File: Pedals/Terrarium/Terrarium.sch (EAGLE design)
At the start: 7 parts, among them U1 ES_DAISY_SEED

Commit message: Updating schematic
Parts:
- added C1: 100p, capacitors-film:CAP.5
- added C100: 100u, capacitors-elec:5.0_MM.4
- added C2, C3, C6: 1u, capacitors-film:CAP.6
- added C4, C5, C8, C9: 100n, capacitors-film:CAP.5
- added C7: 1n, capacitors-film:CAP.5
- added D100: 1N5817, diodes:DO41.3
- added FS1, FS2, SW1, SW2, SW3, SW4: SPST, switches:SPST
- added GND, PWR: PADRD, supply pins:PADRD
- added IC1: TL072CP, SamacSys_Parts:TL072CP
- added IC2: L78L05CZ, SamacSys_Parts:L78L05CZ
- added LED1, LED2: LED.3, diodes:LED.3
- added R5, R8: 1k, SparkFun-Resistors:1KOHM-HORIZ-1/4W-1%
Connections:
- new net +5V: C5.1, C9.1, IC2.VOUT
- new net FS1: FS1.P, U1.GPIO25(ADC10)
- new net FS2: FS2.P, U1.GPIO26(SAI2_SD_A)
- new net IC1_1: IC1.1OUT
- new net IC1_2: IC1.1IN-
- new net IC1_3: IC1.1IN+
- new net IC1_4: IC1.VCC-
- new net IC1_5: IC1.2IN+
- new net IC1_6: IC1.2IN-
- new net IC1_7: IC1.2OUT
- new net IC1_8: IC1.VCC+
- new net LED1: R5.2, U1.GPIO22(ADC7/DAC2)
- new net LED2: R8.2, U1.GPIO23(ADC8/DAC1)
- new net LEFT_IN: U1.AUDIO_IN_L
- new net LEFT_OUT: U1.AUDIO_OUT_L
- new net N$7: LED1.A, R5.1
- new net N$8: LED2.A, R8.1
- new net N$9: D100.A, PWR.P$1
- new net SW1: SW1.P, U1.GPIO10(SPI1_MOSI)
- new net SW2: SW2.P, U1.GPIO9(SPI1_MISO)
- new net SW3: SW3.P, U1.GPIO8(SPI1_SCK)
- new net SW4: SW4.P, U1.GPIO7(SPI1_NSS)
- net GND: now also C100.-, C4.2, C5.2, C8.2, C9.2, FS1.S, FS2.S, GND.P$1, IC2.GND, LED1.C, LED2.C, SW1.S, SW2.S, SW3.S, SW4.S
- net VCC: now also C100.+, C4.1, C8.1, D100.C, IC2.VIN

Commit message: Finish base schematic
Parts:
- added IN, IN_GND, OUT, OUT_GND: PADRD, supply pins:PADRD
- added R1, R2, R3, R9: 1M, resistors:R.3B
- added R4: 100R, resistors:R.3B
- added R6: 100K, resistors:R.3B
- added R7: 1K, resistors:R.3B
- POT1, POT2, POT3, POT4, POT5, POT6: value (none) -> B10K
- R5, R8: value 1k -> 1K; device SparkFun-Resistors:1KOHM-HORIZ-1/4W-1% -> resistors:R.3B
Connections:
- removed net IC1_1: IC1.1OUT
- removed net IC1_2: IC1.1IN-
- removed net IC1_3: IC1.1IN+
- removed net IC1_4: IC1.VCC-
- removed net IC1_5: IC1.2IN+
- removed net IC1_6: IC1.2IN-
- removed net IC1_7: IC1.2OUT
- removed net IC1_8: IC1.VCC+
- new net N$10: C3.2, R4.1
- new net N$11: C3.1, OUT.P$1, R6.1
- new net N$12: C1.1, C6.2, IN.P$1
- new net N$14: IC1.2IN-, IC1.2OUT, R4.2
- new net N$15: C6.1, R7.2
- new net N$16: C7.1, IC1.1IN+, R1.2, R3.1, R7.1
- new net N$17: C2.1, IC1.2IN+, R2.1, R9.2
- net +5V: now also IC1.VCC+, R1.1, R2.2
- net GND: now also C1.2, C7.2, IC1.VCC-, IN_GND.P$1, OUT_GND.P$1, R3.2, R6.2, R9.1
- net LEFT_IN: now also IC1.1IN-, IC1.1OUT
- net LEFT_OUT: now also C2.2
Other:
- moved on the sheet: C1, C100, C2, C3, C4, C5, C6, C7, C8, C9, D100, IC1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

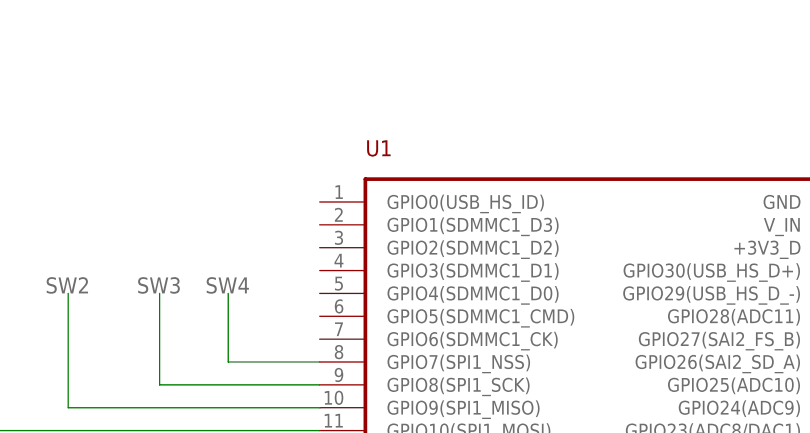
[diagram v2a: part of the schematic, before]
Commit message: Begin board layout
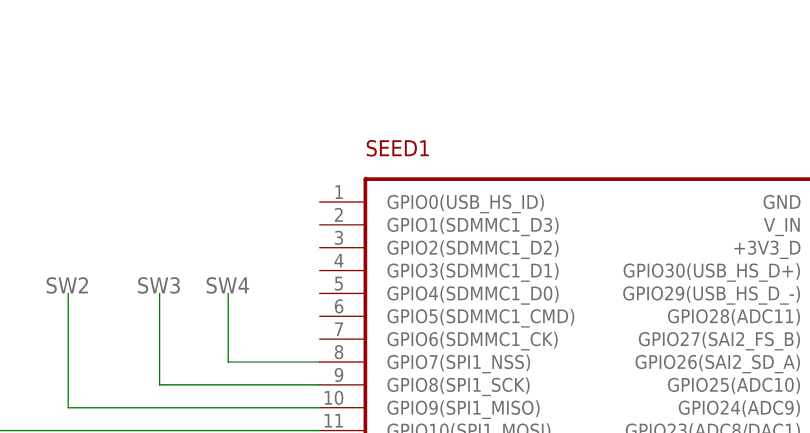
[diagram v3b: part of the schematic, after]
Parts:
- renumbered U1 to SEED1
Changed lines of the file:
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@@
 </classes>
 <parts>
-<part name="U1" library="Electrosmith_Boards" deviceset="ES_DAISY_SEED" device=""/>
+<part name="SEED1" library="Electrosmith_Boards" deviceset="ES_DAISY_SEED" device=""/>
 <part name="GND1" library="SparkFun-PowerSymbols" library_urn="urn:adsk.eagle:library:530" deviceset="GND" device=""/>
 <part name="GND2" library="SparkFun-PowerSymbols" library_urn="urn:adsk.eagle:library:530" deviceset="GND" device=""/>
@@
 </plain>
 <instances>
-<instance part="U1" gate="G$1" x="66.04" y="53.34" smashed="yes">
+<instance part="SEED1" gate="G$1" x="66.04" y="53.34" smashed="yes">
 <attribute name="NAME" x="40.64" y="81.28" size="1.778" layer="94"/>
 <attribute name="VALUE" x="91.44" y="22.86" size="1.778" layer="94" rot="R180"/>
@@
 <segment>
 <wire x1="104.14" y1="81.28" x2="104.14" y2="73.66" width="0.1524" layer="91"/>
-<pinref part="U1" gate="G$1" pin="V_IN"/>
+<pinref part="SEED1" gate="G$1" pin="V_IN"/>
 <wire x1="104.14" y1="73.66" x2="96.52" y2="73.66" width="0.1524" layer="91"/>
 <label x="101.6" y="81.28" size="1.778" layer="95"/>
@@
 <net name="3V3_D" class="0">
 <segment>
-<pinref part="U1" gate="G$1" pin="+3V3_D"/>
+<pinref part="SEED1" gate="G$1" pin="+3V3_D"/>
 <wire x1="96.52" y1="71.12" x2="111.76" y2="71.12" width="0.1524" layer="91"/>
 <wire x1="111.76" y1="71.12" x2="111.76" y2="81.28" width="0.1524" layer="91"/>
@@
 <net name="GND" class="0">
 <segment>
-<pinref part="U1" gate="G$1" pin="GND"/>
+<pinref part="SEED1" gate="G$1" pin="GND"/>
 <wire x1="96.52" y1="76.2" x2="129.54" y2="76.2" width="0.1524" layer="91"/>
 <pinref part="GND1" gate="1" pin="GND"/>
@@
 </segment>
 <segment>
-<pinref part="U1" gate="G$1" pin="AGND"/>
+<pinref part="SEED1" gate="G$1" pin="AGND"/>
 <wire x1="35.56" y1="27.94" x2="27.94" y2="27.94" width="0.1524" layer="91"/>
 <pinref part="GND2" gate="1" pin="GND"/>
@@
 <net name="3V3_A" class="0">
 <segment>
-<pinref part="U1" gate="G$1" pin="+3V3_A"/>
+<pinref part="SEED1" gate="G$1" pin="+3V3_A"/>
 <wire x1="96.52" y1="27.94" x2="111.76" y2="27.94" width="0.1524" layer="91"/>
 <label x="106.68" y="27.94" size="1.778" layer="95"/>
@@
 <net name="N$1" class="0">
 <segment>
-<pinref part="U1" gate="G$1" pin="GPIO16(ADC1)"/>
+<pinref part="SEED1" gate="G$1" pin="GPIO16(ADC1)"/>
 <pinref part="POT1" gate="G$1" pin="2"/>
 <wire x1="96.52" y1="33.02" x2="127" y2="33.02" width="0.1524" layer="91"/>
@@
 <net name="N$2" class="0">
 <segment>
-<pinref part="U1" gate="G$1" pin="GPIO17(ADC2)"/>
+<pinref part="SEED1" gate="G$1" pin="GPIO17(ADC2)"/>
 <pinref part="POT2" gate="G$1" pin="2"/>
 <wire x1="96.52" y1="35.56" x2="142.24" y2="35.56" width="0.1524" layer="91"/>
@@
 <net name="N$3" class="0">
 <segment>
-<pinref part="U1" gate="G$1" pin="GPIO18(ADC3)"/>
+<pinref part="SEED1" gate="G$1" pin="GPIO18(ADC3)"/>
 <pinref part="POT3" gate="G$1" pin="2"/>
 <wire x1="96.52" y1="38.1" x2="157.48" y2="38.1" width="0.1524" layer="91"/>
@@
 <net name="N$4" class="0">
 <segment>
-<pinref part="U1" gate="G$1" pin="GPIO19(ADC4)"/>
+<pinref part="SEED1" gate="G$1" pin="GPIO19(ADC4)"/>
 <pinref part="POT4" gate="G$1" pin="2"/>
 <wire x1="96.52" y1="40.64" x2="172.72" y2="40.64" width="0.1524" layer="91"/>
@@
 <net name="N$5" class="0">
 <segment>
-<pinref part="U1" gate="G$1" pin="GPIO20(ADC5)"/>
+<pinref part="SEED1" gate="G$1" pin="GPIO20(ADC5)"/>
 <pinref part="POT5" gate="G$1" pin="2"/>
 <wire x1="96.52" y1="43.18" x2="187.96" y2="43.18" width="0.1524" layer="91"/>
@@
 <net name="N$6" class="0">
 <segment>
-<pinref part="U1" gate="G$1" pin="GPIO21(ADC6)"/>
+<pinref part="SEED1" gate="G$1" pin="GPIO21(ADC6)"/>
 <pinref part="POT6" gate="G$1" pin="2"/>
 <wire x1="96.52" y1="45.72" x2="205.74" y2="45.72" width="0.1524" layer="91"/>
@@
 <net name="FS2" class="0">
 <segment>
-<pinref part="U1" gate="G$1" pin="GPIO26(SAI2_SD_A)"/>
+<pinref part="SEED1" gate="G$1" pin="GPIO26(SAI2_SD_A)"/>
 <wire x1="96.52" y1="58.42" x2="101.6" y2="58.42" width="0.1524" layer="91"/>
 <wire x1="101.6" y1="58.42" x2="101.6" y2="63.5" width="0.1524" layer="91"/>
@@
 <net name="FS1" class="0">
 <segment>
-<pinref part="U1" gate="G$1" pin="GPIO25(ADC10)"/>
+<pinref part="SEED1" gate="G$1" pin="GPIO25(ADC10)"/>
 <wire x1="96.52" y1="55.88" x2="106.68" y2="55.88" width="0.1524" layer="91"/>
 <wire x1="106.68" y1="55.88" x2="106.68" y2="63.5" width="0.1524" layer="91"/>
@@
 <net name="LED2" class="0">
 <segment>
-<pinref part="U1" gate="G$1" pin="GPIO23(ADC8/DAC1)"/>
+<pinref part="SEED1" gate="G$1" pin="GPIO23(ADC8/DAC1)"/>
 <wire x1="96.52" y1="50.8" x2="114.3" y2="50.8" width="0.1524" layer="91"/>
 <wire x1="114.3" y1="50.8" x2="114.3" y2="63.5" width="0.1524" layer="91"/>
@@
 <net name="LED1" class="0">
 <segment>
-<pinref part="U1" gate="G$1" pin="GPIO22(ADC7/DAC2)"/>
+<pinref part="SEED1" gate="G$1" pin="GPIO22(ADC7/DAC2)"/>
 <wire x1="96.52" y1="48.26" x2="121.92" y2="48.26" width="0.1524" layer="91"/>
 <wire x1="121.92" y1="48.26" x2="121.92" y2="63.5" width="0.1524" layer="91"/>
@@
 <net name="LEFT_OUT" class="0">
 <segment>
-<pinref part="U1" gate="G$1" pin="AUDIO_OUT_L"/>
+<pinref part="SEED1" gate="G$1" pin="AUDIO_OUT_L"/>
 <wire x1="35.56" y1="33.02" x2="10.16" y2="33.02" width="0.1524" layer="91"/>
 <label x="5.08" y="33.02" size="1.778" layer="95"/>
@@
 <net name="LEFT_IN" class="0">
 <segment>
-<pinref part="U1" gate="G$1" pin="AUDIO_IN_L"/>
+<pinref part="SEED1" gate="G$1" pin="AUDIO_IN_L"/>
 <wire x1="35.56" y1="38.1" x2="10.16" y2="38.1" width="0.1524" layer="91"/>
 <label x="5.08" y="38.1" size="1.778" layer="95"/>
@@
 <net name="SW4" class="0">
 <segment>
-<pinref part="U1" gate="G$1" pin="GPIO7(SPI1_NSS)"/>
+<pinref part="SEED1" gate="G$1" pin="GPIO7(SPI1_NSS)"/>
 <wire x1="35.56" y1="58.42" x2="25.4" y2="58.42" width="0.1524" layer="91"/>
 <wire x1="25.4" y1="58.42" x2="25.4" y2="66.04" width="0.1524" layer="91"/>
@@
 <net name="SW3" class="0">
 <segment>
-<pinref part="U1" gate="G$1" pin="GPIO8(SPI1_SCK)"/>
+<pinref part="SEED1" gate="G$1" pin="GPIO8(SPI1_SCK)"/>
 <wire x1="35.56" y1="55.88" x2="17.78" y2="55.88" width="0.1524" layer="91"/>
 <wire x1="17.78" y1="55.88" x2="17.78" y2="66.04" width="0.1524" layer="91"/>
@@
 <net name="SW2" class="0">
 <segment>
-<pinref part="U1" gate="G$1" pin="GPIO9(SPI1_MISO)"/>
+<pinref part="SEED1" gate="G$1" pin="GPIO9(SPI1_MISO)"/>
 <wire x1="35.56" y1="53.34" x2="7.62" y2="53.34" width="0.1524" layer="91"/>
 <wire x1="7.62" y1="53.34" x2="7.62" y2="66.04" width="0.1524" layer="91"/>
@@
 <net name="SW1" class="0">
 <segment>
-<pinref part="U1" gate="G$1" pin="GPIO10(SPI1_MOSI)"/>
+<pinref part="SEED1" gate="G$1" pin="GPIO10(SPI1_MOSI)"/>
 <wire x1="35.56" y1="50.8" x2="-2.54" y2="50.8" width="0.1524" layer="91"/>
 <wire x1="-2.54" y1="50.8" x2="-2.54" y2="66.04" width="0.1524" layer="91"/>

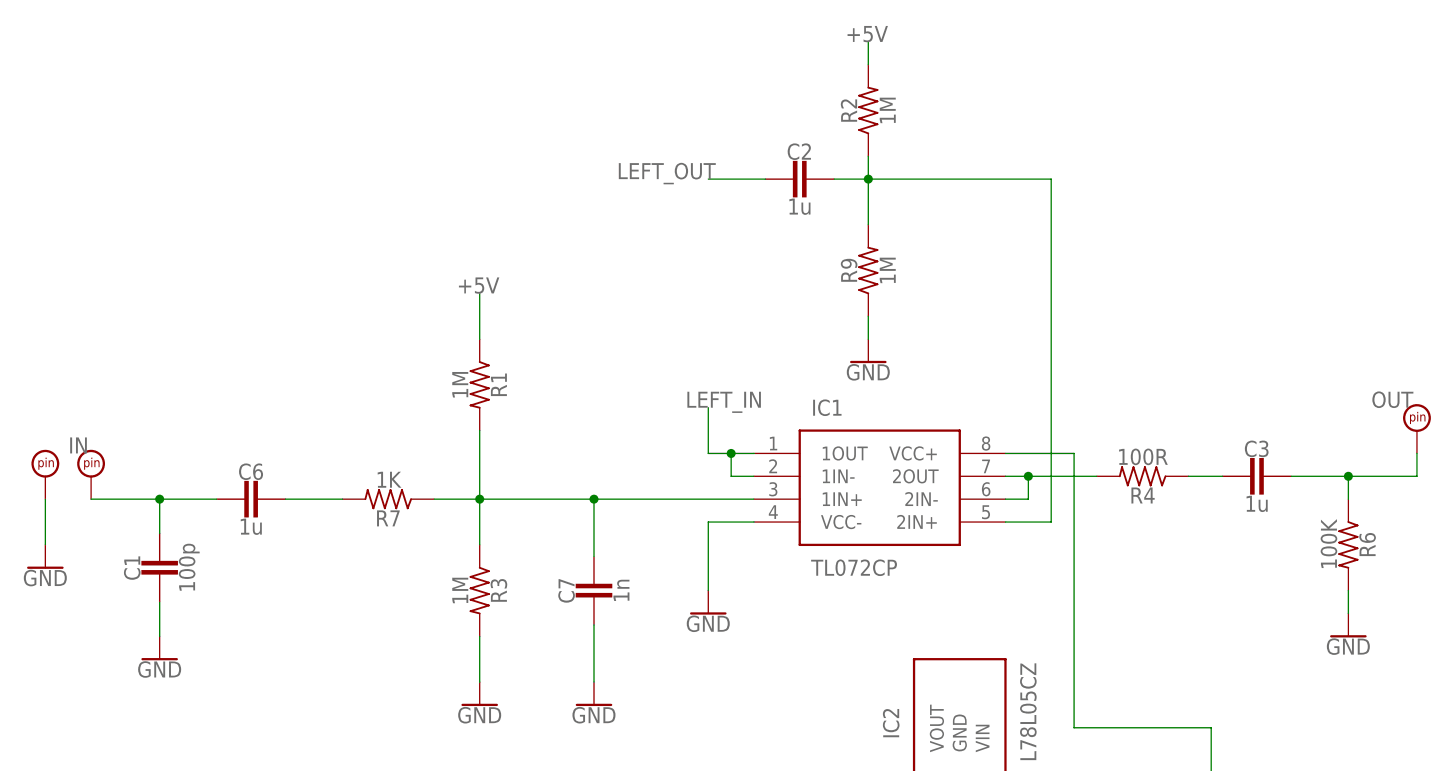
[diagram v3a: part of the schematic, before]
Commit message: Fix capacitor sizes
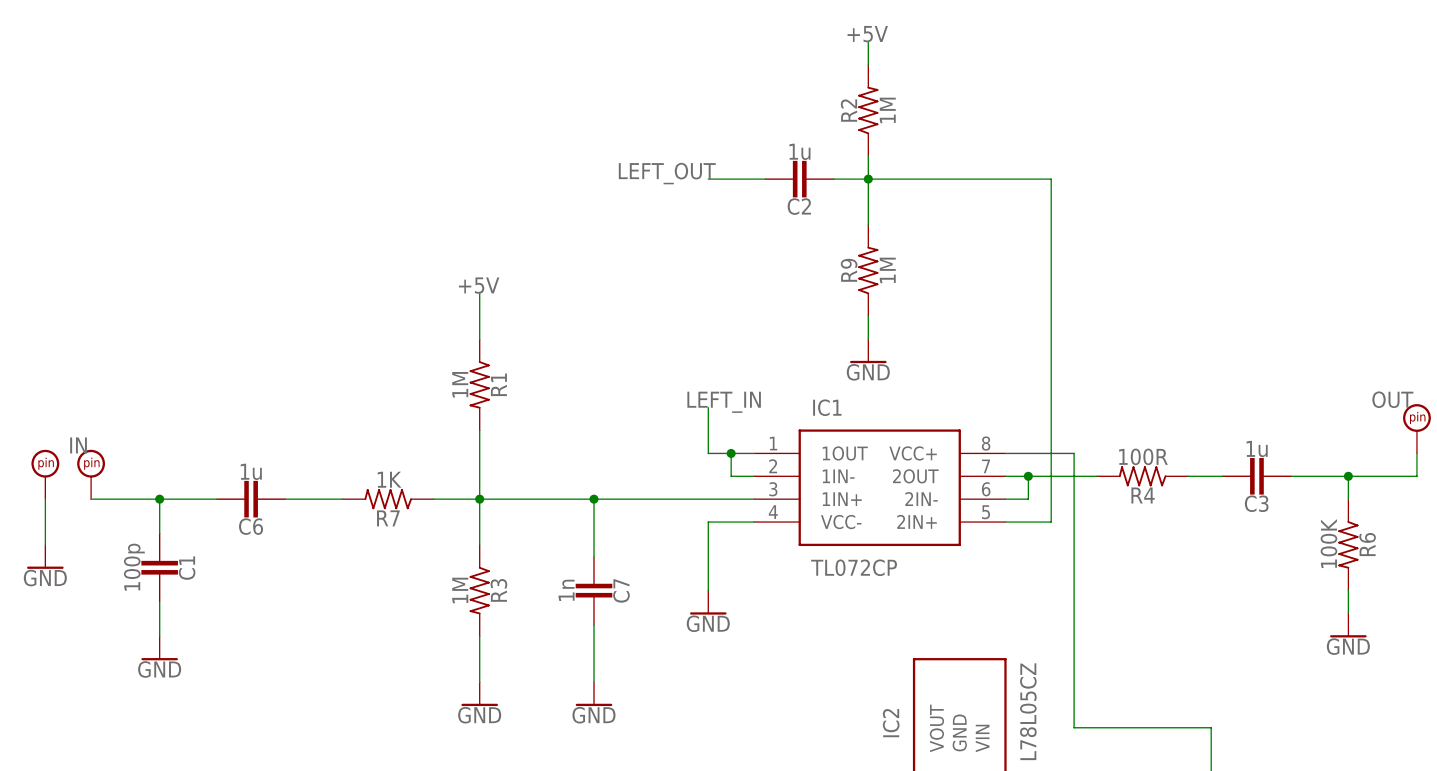
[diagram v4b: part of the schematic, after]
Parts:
- C1, C4, C5, C7, C8, C9: device capacitors-film:CAP.5 -> capacitors-film:CAP.2
- C2, C3, C6: device capacitors-film:CAP.6 -> capacitors-film:CAP.5
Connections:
- net GND: now also C1.1, C7.1; no longer C1.2, C7.2
- net LEFT_OUT: now also C2.1; no longer C2.2
- net N$10: now also C3.1; no longer C3.2
- net N$11: now also C3.2; no longer C3.1
- net N$12: now also C1.2, C6.1; no longer C1.1, C6.2
- net N$15: now also C6.2; no longer C6.1
- net N$16: now also C7.2; no longer C7.1
- net N$17: now also C2.2; no longer C2.1
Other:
- moved on the sheet: C1, C2, C3, C6, C7

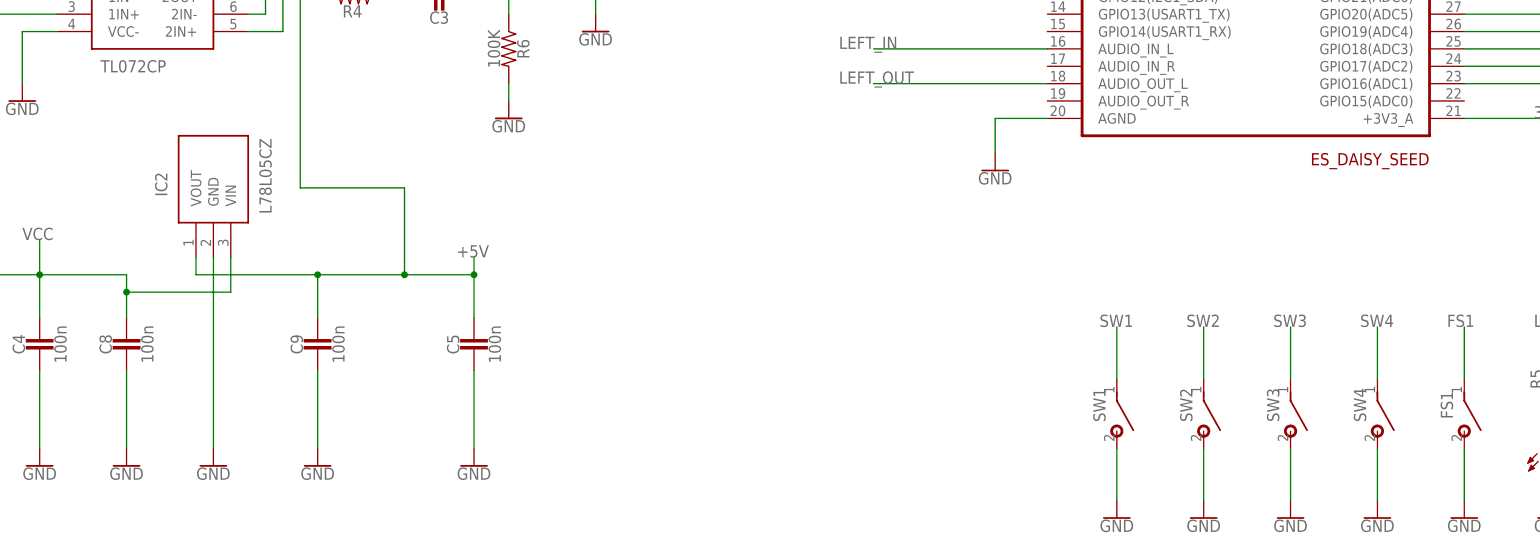
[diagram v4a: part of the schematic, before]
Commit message: Update parts and place them on the board
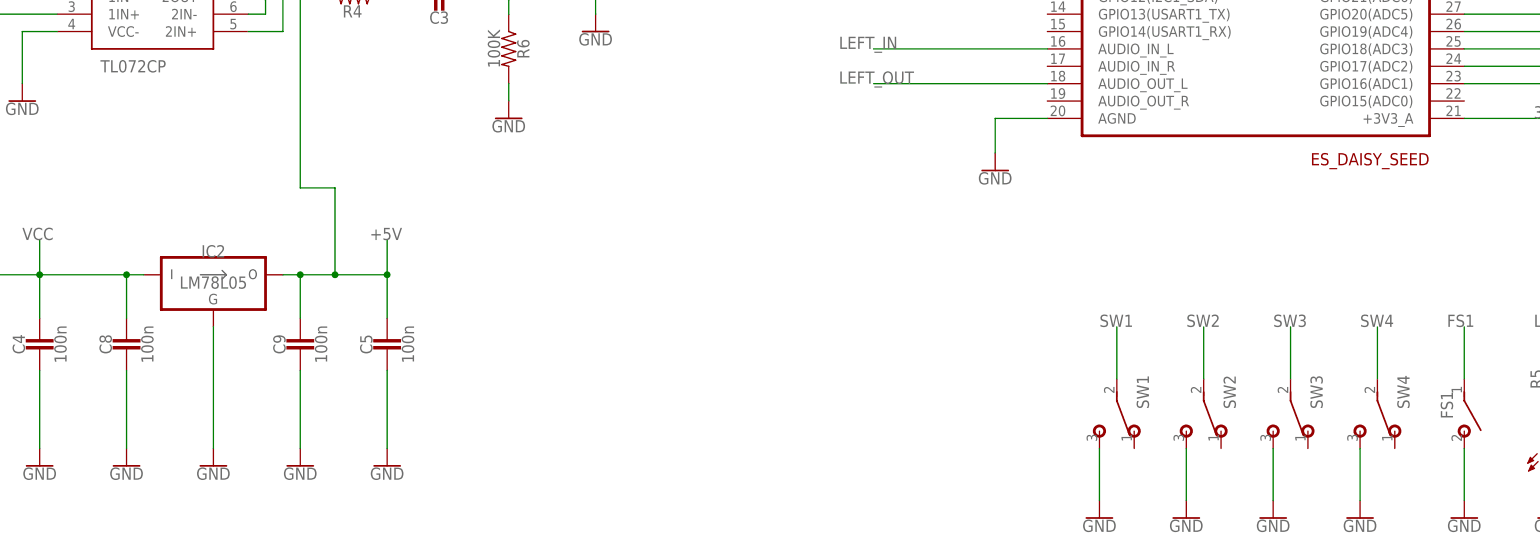
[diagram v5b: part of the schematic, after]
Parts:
- IC2: value L78L05CZ -> LM78L05; device SamacSys_Parts:L78L05CZ -> regulators:LM78L05
- SW1, SW2, SW3, SW4: value SPST -> (none); device switches:SPST -> switches:SPDT.1
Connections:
- net +5V: now also IC2.VO; no longer IC2.VOUT
- net VCC: now also IC2.VI; no longer IC2.VIN
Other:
- moved on the sheet: C5, C9, IC2
